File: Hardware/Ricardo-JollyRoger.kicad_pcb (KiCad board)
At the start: 4 copper layers, 45.1 x 35.1 mm, 87 parts, among them J1 RBUS, J2 USB_C_Receptacle_USB2.0, J3 Conn_01x08_Pin, U1 ESP32-S3, U2 SN65HVD230, U3 LM66200DRLR, U4 MAX77827AEFD+T, U5 SC4215ASTRT, U7 LM66200DRLR, Y1 R940000171

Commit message: Increase board size
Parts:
- moved H2 0.99 mm to (121.6, 48.4)
- moved H1 0.70 mm to (82.4, 48.4)
- moved H3 0.70 mm to (121.6, 77.6)
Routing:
- net /NAND_CLK: track 38.1 -> 15.1 mm, vias 1 -> 0
- net /NAND_CMD: track 35.8 -> 12.9 mm, vias 1 -> 0
- net /NAND_SD2: track 35.8 -> 12.9 mm, vias 1 -> 0
- net /NAND_SD3: track 35.8 -> 13.0 mm, vias 1 -> 0
- net /NAND_SD1: track 35.8 -> 13.0 mm, vias 1 -> 0
- net /NAND_SD0: track 35.7 -> 13.0 mm, vias 1 -> 0
- net /HEADER_3V3: track 19.5 -> 1.38 mm
- net /NAND_3V3: track 13.8 -> 4.58 mm, vias 2 -> 0
- net GND: vias 61 -> 59
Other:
- board size 45.1 x 35.1 mm -> 45.8 x 35.8 mm

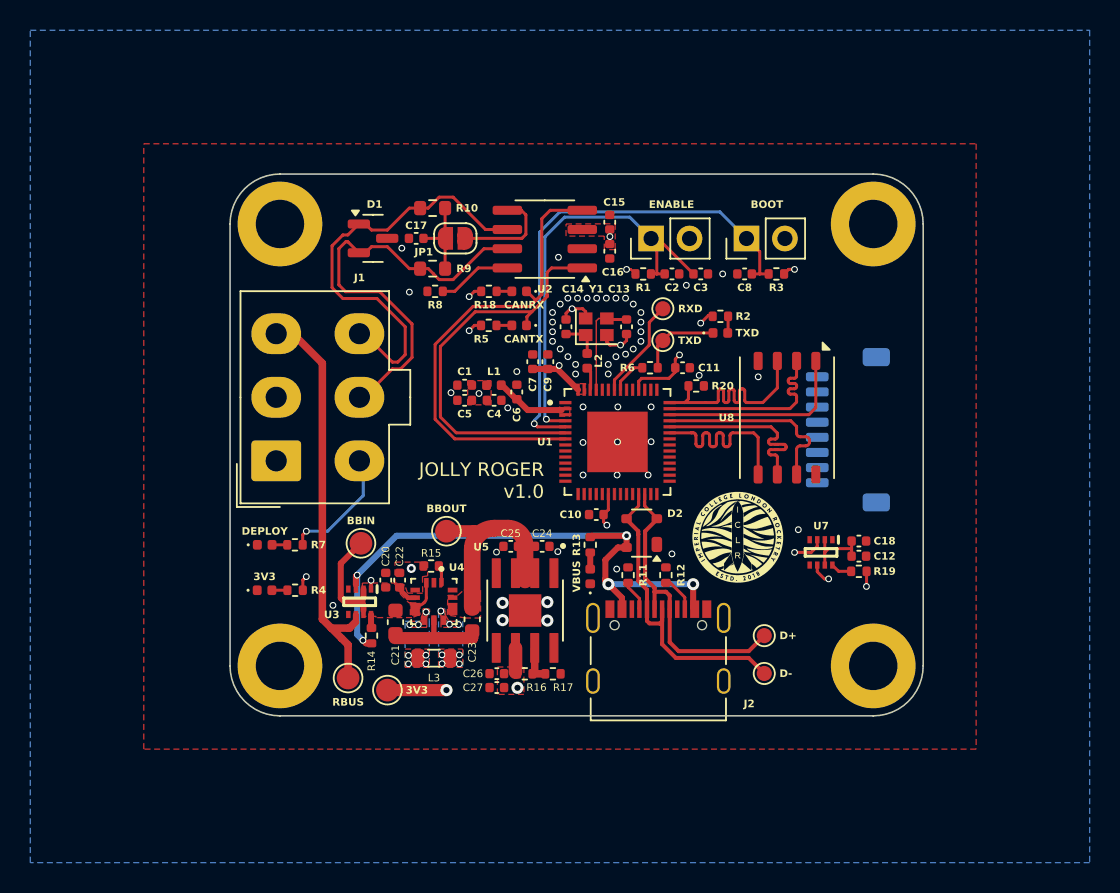
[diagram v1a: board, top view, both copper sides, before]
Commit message: Added edge vias
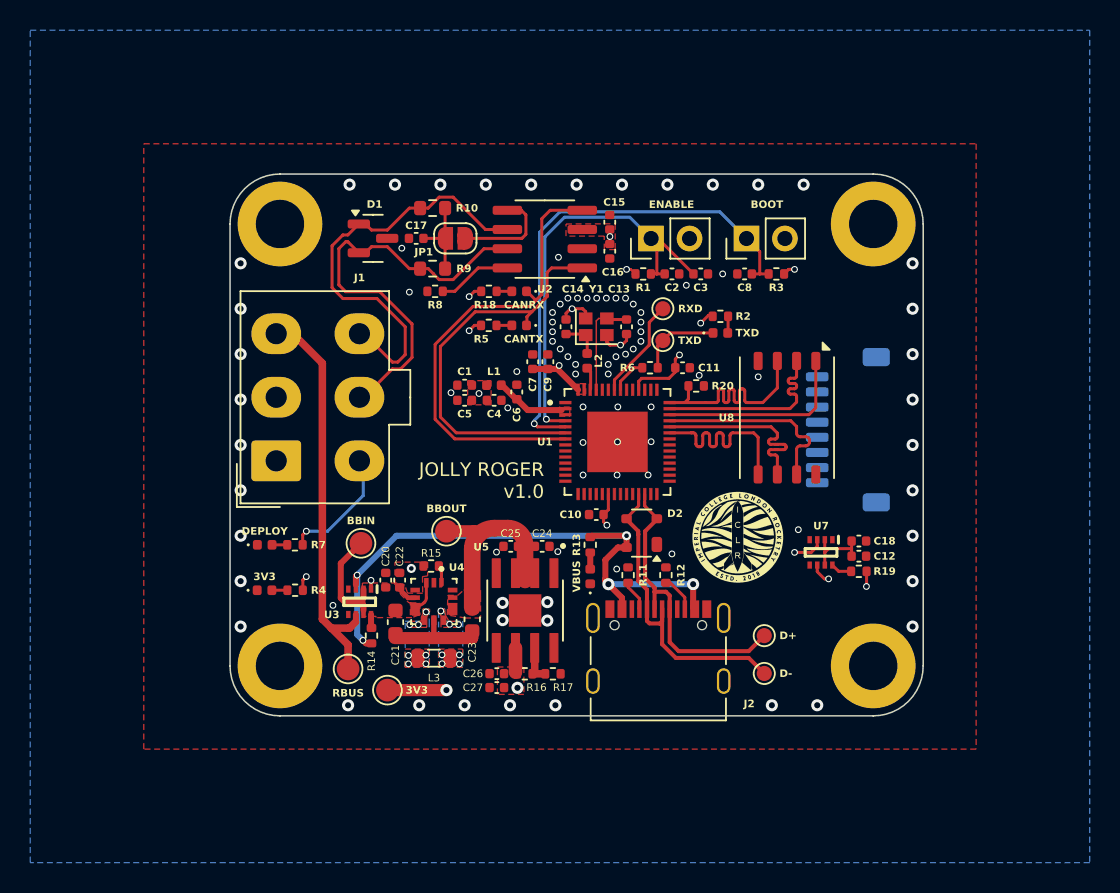
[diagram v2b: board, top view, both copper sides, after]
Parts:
- moved RBUS 0.60 mm to (86.9, 77.8)
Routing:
- net RBUS_uC_V: track 27.6 -> 27.0 mm
- net GND: vias 59 -> 95

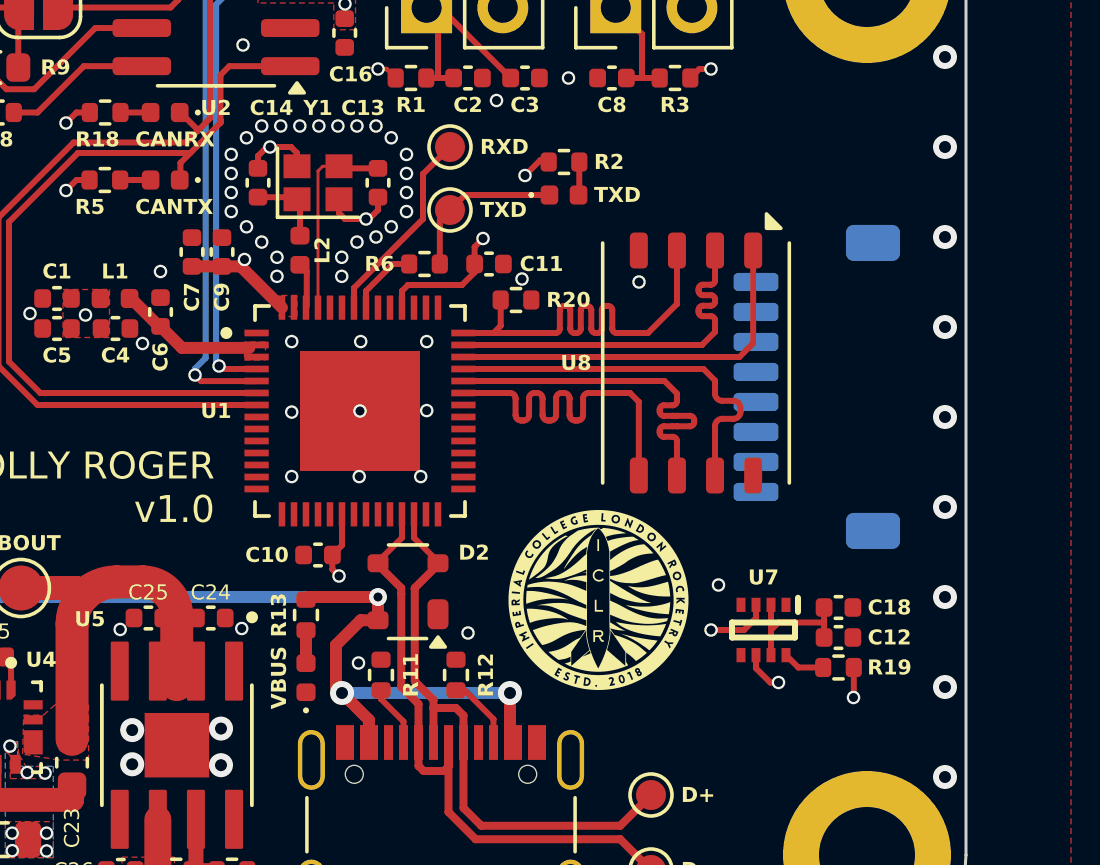
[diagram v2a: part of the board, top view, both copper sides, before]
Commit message: Updated NAND traces
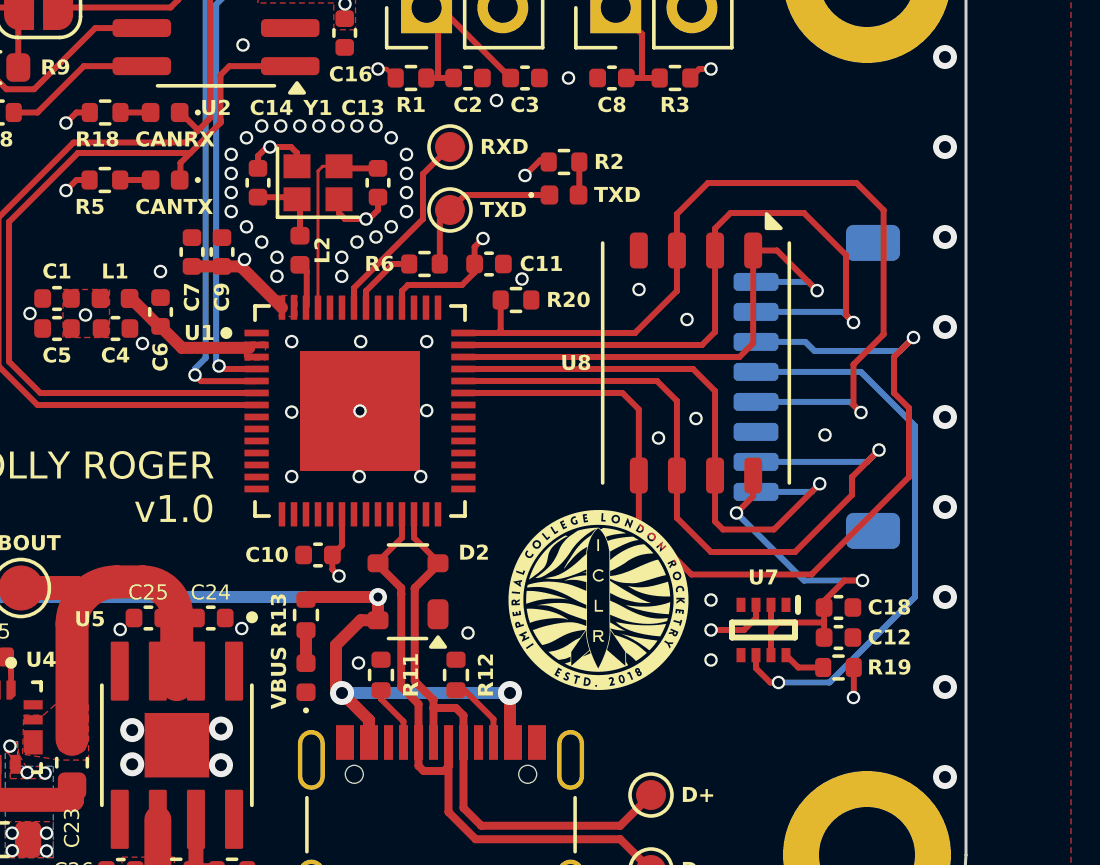
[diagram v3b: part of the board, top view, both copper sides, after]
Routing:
- net /NAND_CMD: track 12.9 -> 31.6 mm, vias 0 -> 1
- net /HEADER_3V3: track 1.38 -> 18.9 mm
- net /NAND_CLK: track 15.1 -> 30.0 mm, vias 0 -> 1
- net /NAND_SD0: track 13.0 -> 24.5 mm, vias 0 -> 1
- net /NAND_SD3: track 13.0 -> 22.9 mm, vias 0 -> 1
- net /NAND_3V3: track 4.58 -> 13.0 mm, vias 0 -> 2
- net /NAND_SD1: track 13.0 -> 19.5 mm, vias 0 -> 1
- net /NAND_SD2: track 12.9 -> 17.8 mm, vias 0 -> 1
- net GND: vias 95 -> 100

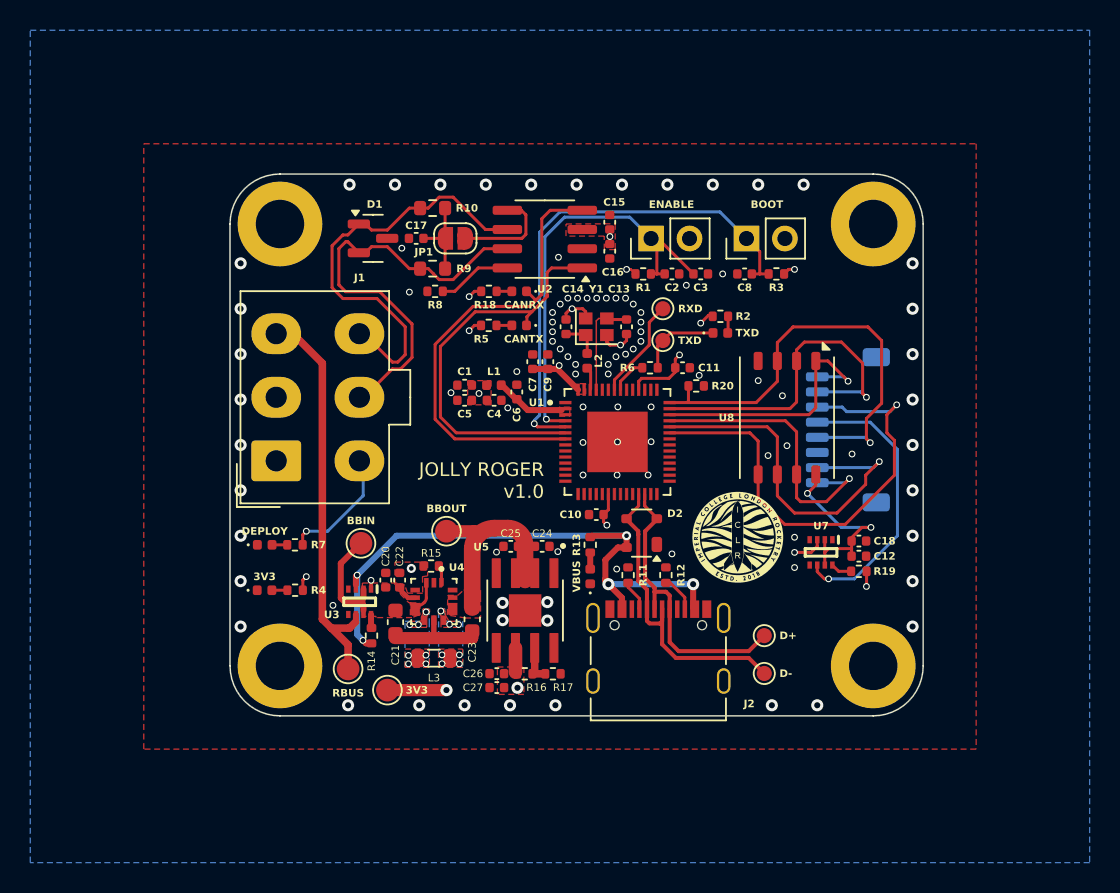
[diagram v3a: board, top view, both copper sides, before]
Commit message: Added standalone labels for named components
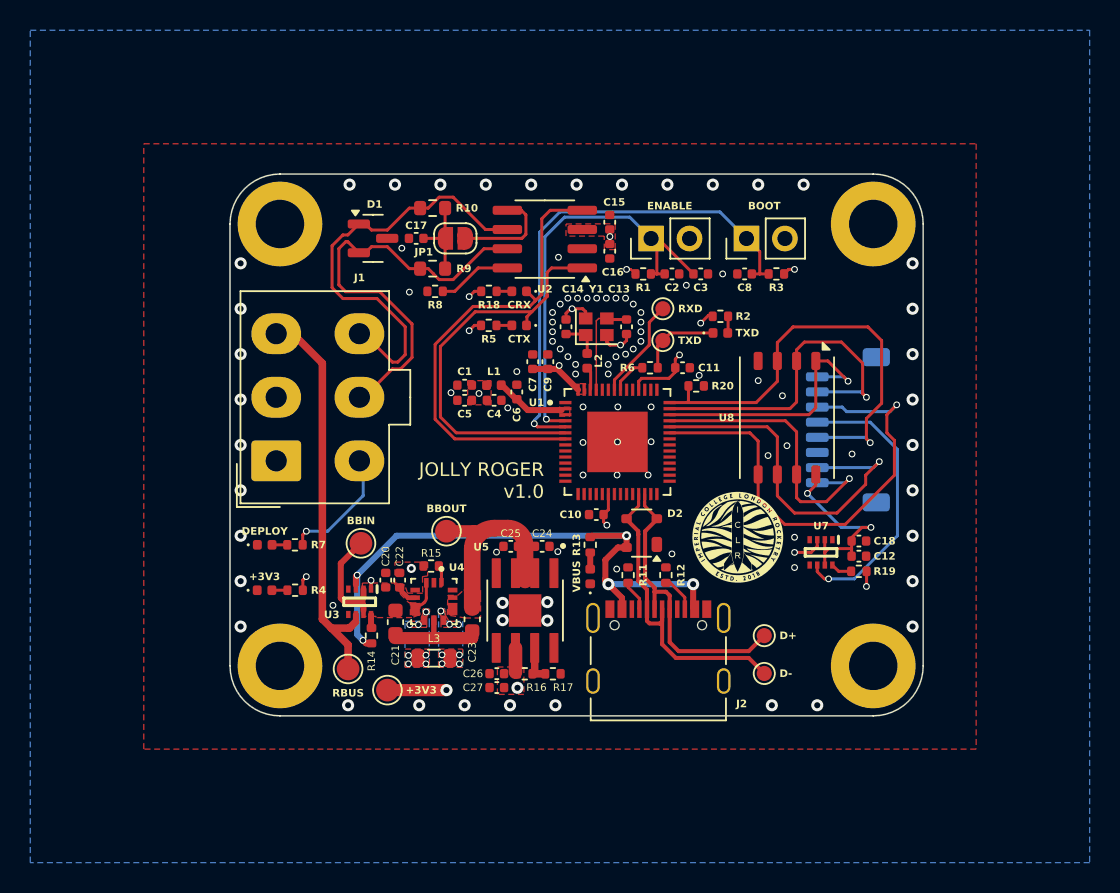
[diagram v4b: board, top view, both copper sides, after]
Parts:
- renumbered DEPLOY to 12VLED1, 3V3 to 3V3LED1, BOOT to BOOTJUMPER1, CANRX to CRXLED1, CANTX to CTXLED1, ENABLE to ENJUMPER1, D- to TP1, RXD to TP10, D+ to TP2, BBIN to TP4, RBUS to TP5, 3V3 to TP6, BBOUT to TP8, TXD to TP9, TXD to TXLED1, VBUS to USBLED1
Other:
- board text added: "+3V3"
- board text added: "BBIN"
- board text added: "BBOUT"
- board text added: "BOOT"
- board text added: "CRX"
- board text added: "CTX"
- board text added: "D+"
- board text added: "D-"
- board text added: "DEPLOY"
- board text added: "ENABLE"
- board text added: "RBUS"
- board text added: "RXD"
- board text added: "TXD"
- board text added: "VBUS"

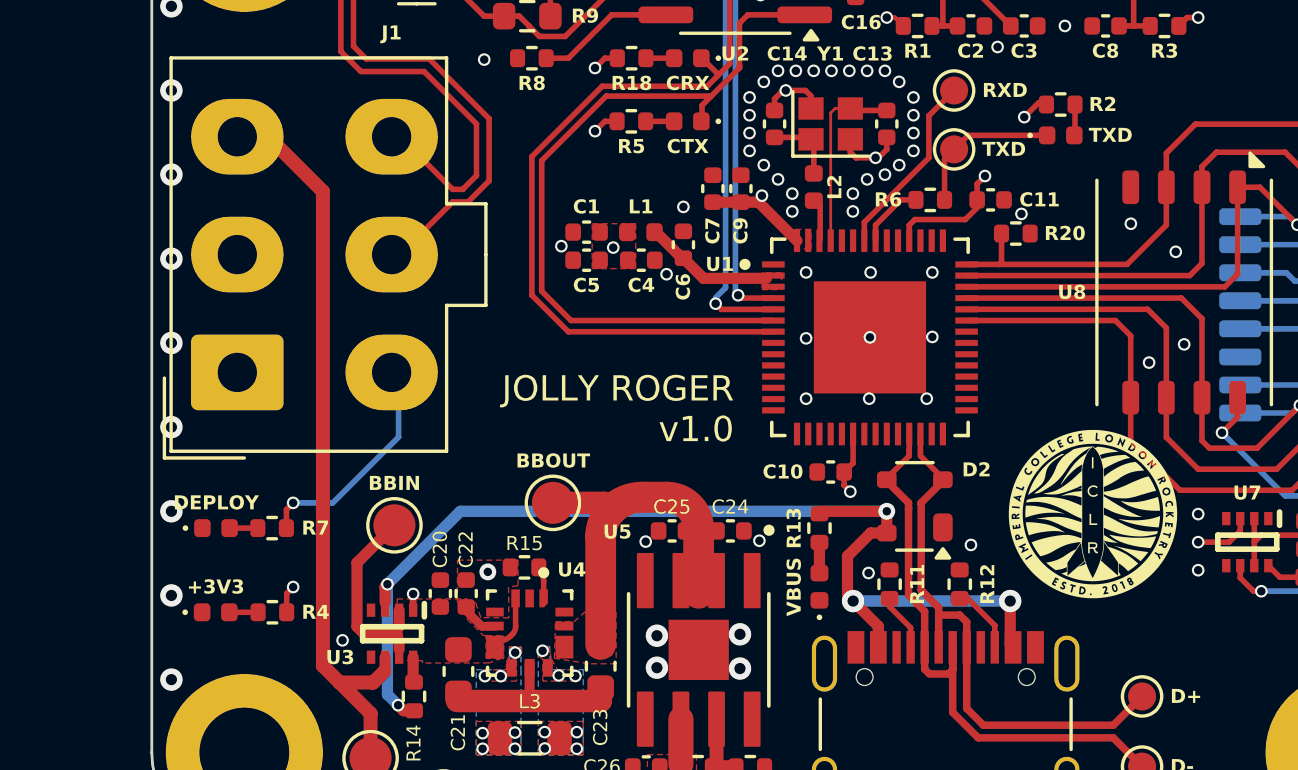
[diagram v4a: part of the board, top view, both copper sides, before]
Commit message: Updated NAND termination resistor
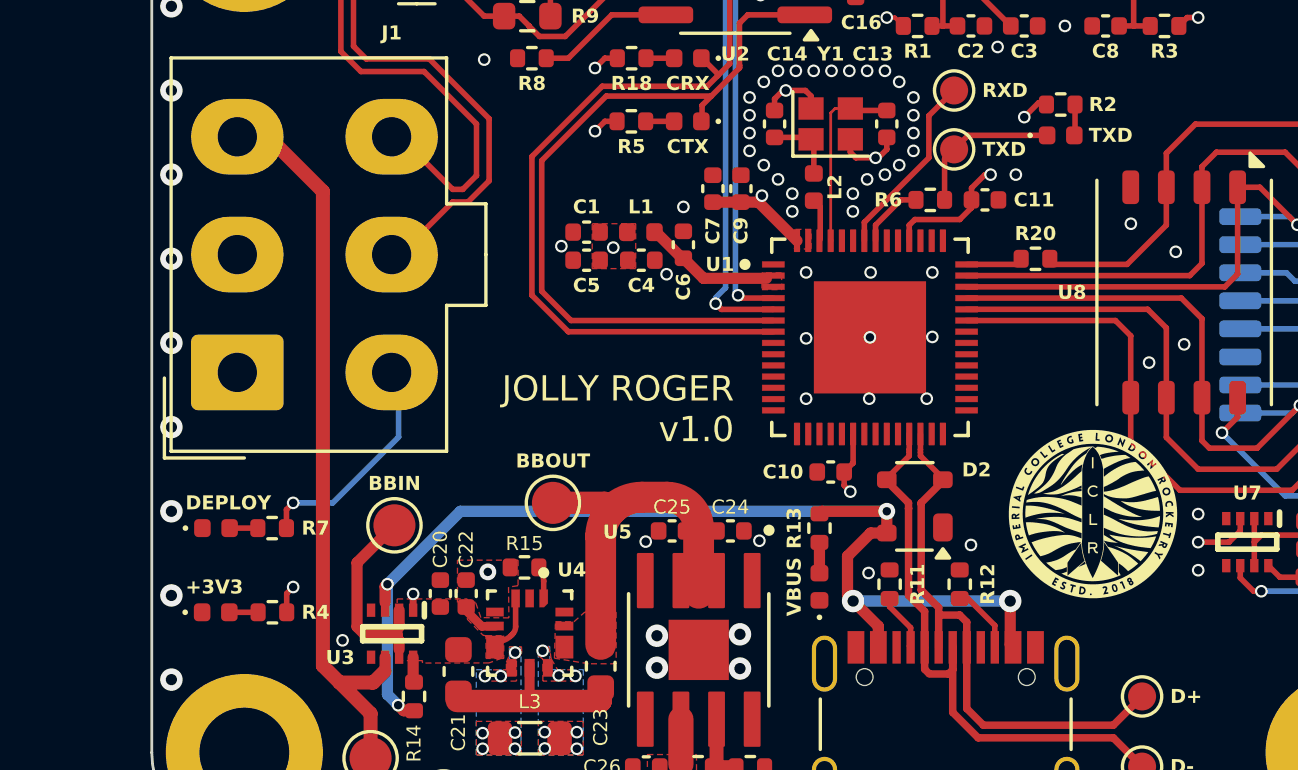
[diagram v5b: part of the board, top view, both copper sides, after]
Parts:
- R20: value R -> 33
- moved R20 1.14 mm to (110.6, 60.0)
- moved C11 0.20 mm to (108.8, 57.9)
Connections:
- R20 pad 1: /NAND_CLK -> Net-(U1-GPIO37)
- R20 pad 2: GND -> /NAND_CLK
- U1 pad 42: /NAND_CLK -> Net-(U1-GPIO37)
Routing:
- net /NAND_CLK: track 30.0 -> 26.0 mm
- net Net-(U1-GPIO37): track 0.00 -> 2.03 mm
